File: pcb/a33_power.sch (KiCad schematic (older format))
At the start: 48 parts, among them U3 TPS62095RGTR, U4 TPS62095RGTR, U5 TPS62095RGTR, U6 TPS62095RGTR

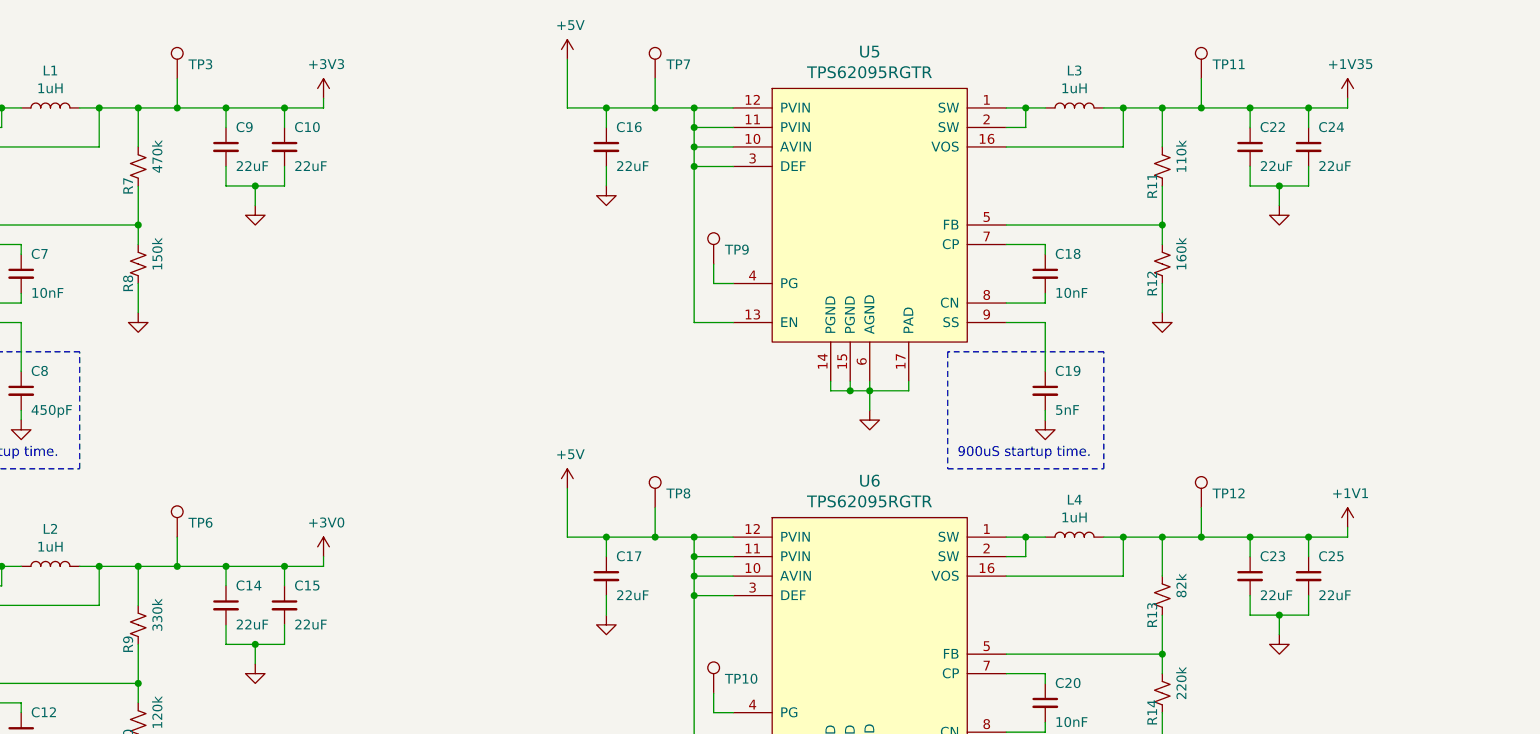
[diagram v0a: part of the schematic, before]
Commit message: Finished up all the switching power supplies.
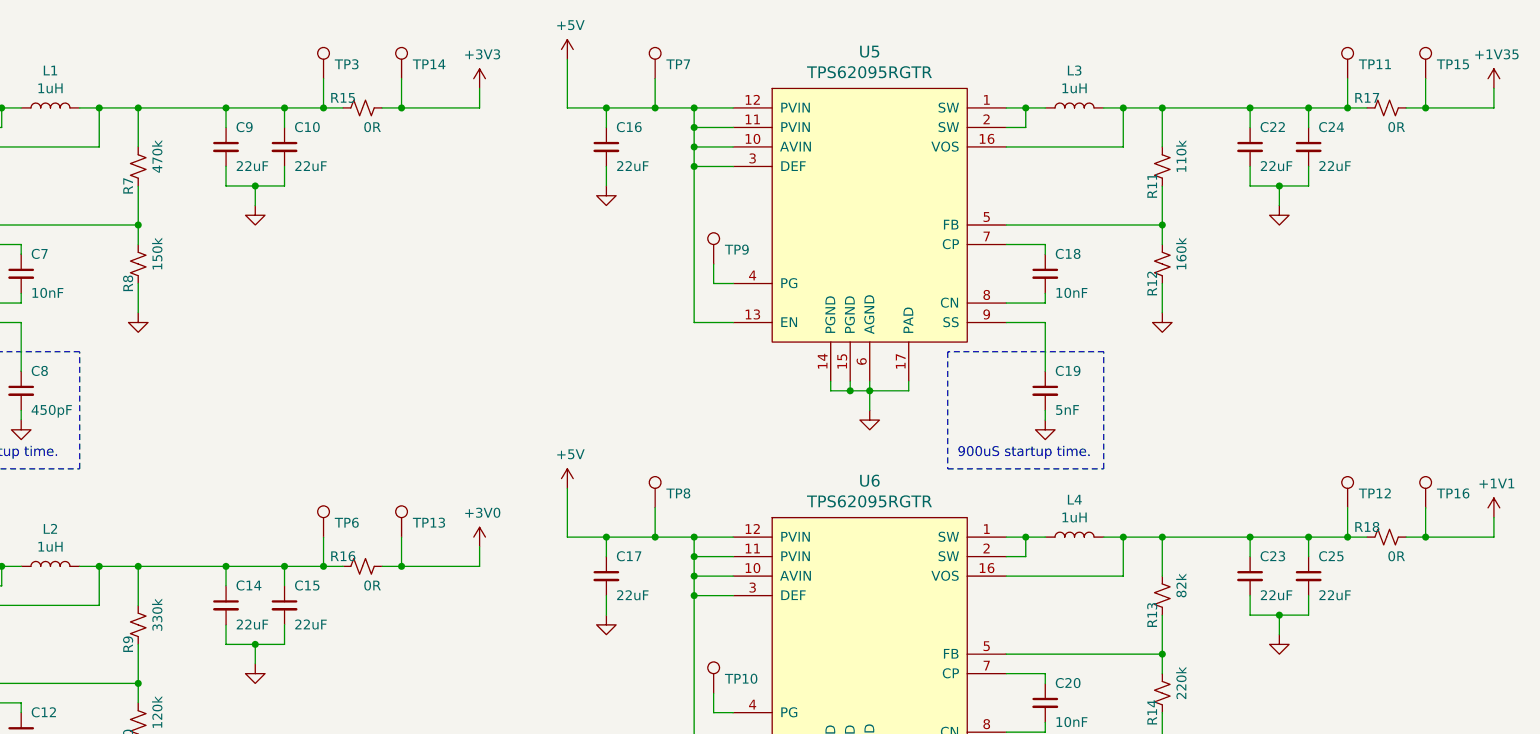
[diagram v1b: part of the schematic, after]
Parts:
- added R15, R16, R17, R18: 0R, Resistor_SMD:R_0402_1005Metric, symbol Device:R_Small_US
- added TP13, TP14, TP15, TP16: TestPoint, symbol Connector:TestPoint
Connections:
- net +1V1: now also R18.1, TP16.1; no longer C23.1, C25.1, L4.2, R13.1, TP12.1, U6.16 (VOS)
- net +1V35: now also R17.1, TP15.1; no longer C22.1, C24.1, L3.2, R11.1, TP11.1, U5.16 (VOS)
- net +3V0: now also R16.1, TP13.1; no longer C14.1, C15.1, L2.2, R9.1, TP6.1, U4.16 (VOS)
- net +3V3: now also R15.1, TP14.1; no longer C10.1, C9.1, L1.2, R7.1, TP3.1, U3.16 (VOS)
- new net: C10.1, C9.1, L1.2, R15.2, R7.1, TP3.1, U3.16 (VOS)
- new net: C14.1, C15.1, L2.2, R16.2, R9.1, TP6.1, U4.16 (VOS)
- new net: C22.1, C24.1, L3.2, R11.1, R17.2, TP11.1, U5.16 (VOS)
- new net: C23.1, C25.1, L4.2, R13.1, R18.2, TP12.1, U6.16 (VOS)
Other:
- moved on the sheet: TP11, TP12, TP3, TP6

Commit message: Added the inductor PN in and dropped them on the board.
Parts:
- L1, L3, L4: footprint (none) -> Inductor_SMD:L_Coilcraft_XxL4020; Part Number (none) -> XAL4020-102ME
- L2: footprint (none) -> Inductor_SMD:L_Coilcraft_XxL4020; Part Nunber (none) -> XAL4020-102ME
- TP1, TP10, TP11, TP12, TP13, TP14, TP15, TP16, TP2, TP3, TP4, TP5, TP6, TP7, TP8, TP9: footprint (none) -> TestPoint:TestPoint_Pad_1.0x1.0mm
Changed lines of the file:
@@
 F 0 "TP2" H 1508 1872 50  0000 L CNN
 F 1 "TestPoint" H 1508 1827 50  0001 L CNN
-F 2 "" H 1650 1800 50  0001 C CNN
+F 2 "TestPoint:TestPoint_Pad_1.0x1.0mm" H 1650 1800 50  0001 C CNN
 F 3 "~" H 1650 1800 50  0001 C CNN
 	1    1450 1800
@@
 F 0 "L1" V 3490 1000 50  0000 C CNN
 F 1 "1uH" V 3399 1000 50  0000 C CNN
-F 2 "" H 3300 1000 50  0001 C CNN
+F 2 "Inductor_SMD:L_Coilcraft_XxL4020" H 3300 1000 50  0001 C CNN
 F 3 "~" H 3300 1000 50  0001 C CNN
+F 4 "XAL4020-102ME" V 3300 1000 50  0001 C CNN "Part Number"
 	1    3300 1000
 	0    -1   -1   0
@@
 F 0 "TP3" H 4758 922 50  0000 L CNN
 F 1 "TestPoint" H 4758 877 50  0001 L CNN
-F 2 "" H 4900 850 50  0001 C CNN
+F 2 "TestPoint:TestPoint_Pad_1.0x1.0mm" H 4900 850 50  0001 C CNN
 F 3 "~" H 4900 850 50  0001 C CNN
 	1    4700 850
@@
 F 0 "TP1" H 1208 922 50  0000 L CNN
 F 1 "TestPoint" H 1208 877 50  0001 L CNN
-F 2 "" H 1350 850 50  0001 C CNN
+F 2 "TestPoint:TestPoint_Pad_1.0x1.0mm" H 1350 850 50  0001 C CNN
 F 3 "~" H 1350 850 50  0001 C CNN
 	1    1150 850
@@
 F 0 "TP5" H 1508 4222 50  0000 L CNN
 F 1 "TestPoint" H 1508 4177 50  0001 L CNN
-F 2 "" H 1650 4150 50  0001 C CNN
+F 2 "TestPoint:TestPoint_Pad_1.0x1.0mm" H 1650 4150 50  0001 C CNN
 F 3 "~" H 1650 4150 50  0001 C CNN
 	1    1450 4150
@@
 F 0 "L2" V 3490 3350 50  0000 C CNN
 F 1 "1uH" V 3399 3350 50  0000 C CNN
-F 2 "" H 3300 3350 50  0001 C CNN
+F 2 "Inductor_SMD:L_Coilcraft_XxL4020" H 3300 3350 50  0001 C CNN
 F 3 "~" H 3300 3350 50  0001 C CNN
+F 4 "XAL4020-102ME" V 3300 3350 50  0001 C CNN "Part Nunber"
 	1    3300 3350
 	0    -1   -1   0
@@
 F 0 "TP6" H 4758 3272 50  0000 L CNN
 F 1 "TestPoint" H 4758 3227 50  0001 L CNN
-F 2 "" H 4900 3200 50  0001 C CNN
+F 2 "TestPoint:TestPoint_Pad_1.0x1.0mm" H 4900 3200 50  0001 C CNN
 F 3 "~" H 4900 3200 50  0001 C CNN
 	1    4700 3200
@@
 F 0 "TP4" H 1208 3272 50  0000 L CNN
 F 1 "TestPoint" H 1208 3227 50  0001 L CNN
-F 2 "" H 1350 3200 50  0001 C CNN
+F 2 "TestPoint:TestPoint_Pad_1.0x1.0mm" H 1350 3200 50  0001 C CNN
 F 3 "~" H 1350 3200 50  0001 C CNN
 	1    1150 3200
@@
 F 0 "TP9" H 6758 1872 50  0000 L CNN
 F 1 "TestPoint" H 6758 1827 50  0001 L CNN
-F 2 "" H 6900 1800 50  0001 C CNN
+F 2 "TestPoint:TestPoint_Pad_1.0x1.0mm" H 6900 1800 50  0001 C CNN
 F 3 "~" H 6900 1800 50  0001 C CNN
 	1    6700 1800
@@
 F 0 "L3" V 8740 1000 50  0000 C CNN
 F 1 "1uH" V 8649 1000 50  0000 C CNN
-F 2 "" H 8550 1000 50  0001 C CNN
+F 2 "Inductor_SMD:L_Coilcraft_XxL4020" H 8550 1000 50  0001 C CNN
 F 3 "~" H 8550 1000 50  0001 C CNN
+F 4 "XAL4020-102ME" V 8550 1000 50  0001 C CNN "Part Number"
 	1    8550 1000
 	0    -1   -1   0
@@
 F 0 "TP11" H 10008 922 50  0000 L CNN
 F 1 "TestPoint" H 10008 877 50  0001 L CNN
-F 2 "" H 10150 850 50  0001 C CNN
+F 2 "TestPoint:TestPoint_Pad_1.0x1.0mm" H 10150 850 50  0001 C CNN
 F 3 "~" H 10150 850 50  0001 C CNN
 	1    9950 850
@@
 F 0 "TP7" H 6458 922 50  0000 L CNN
 F 1 "TestPoint" H 6458 877 50  0001 L CNN
-F 2 "" H 6600 850 50  0001 C CNN
+F 2 "TestPoint:TestPoint_Pad_1.0x1.0mm" H 6600 850 50  0001 C CNN
 F 3 "~" H 6600 850 50  0001 C CNN
 	1    6400 850
@@
 F 0 "TP10" H 6758 4072 50  0000 L CNN
 F 1 "TestPoint" H 6758 4027 50  0001 L CNN
-F 2 "" H 6900 4000 50  0001 C CNN
+F 2 "TestPoint:TestPoint_Pad_1.0x1.0mm" H 6900 4000 50  0001 C CNN
 F 3 "~" H 6900 4000 50  0001 C CNN
 	1    6700 4000
@@
 F 0 "L4" V 8740 3200 50  0000 C CNN
 F 1 "1uH" V 8649 3200 50  0000 C CNN
-F 2 "" H 8550 3200 50  0001 C CNN
+F 2 "Inductor_SMD:L_Coilcraft_XxL4020" H 8550 3200 50  0001 C CNN
 F 3 "~" H 8550 3200 50  0001 C CNN
+F 4 "XAL4020-102ME" V 8550 3200 50  0001 C CNN "Part Number"
 	1    8550 3200
 	0    -1   -1   0
@@
 F 0 "TP12" H 10008 3122 50  0000 L CNN
 F 1 "TestPoint" H 10008 3077 50  0001 L CNN
-F 2 "" H 10150 3050 50  0001 C CNN
+F 2 "TestPoint:TestPoint_Pad_1.0x1.0mm" H 10150 3050 50  0001 C CNN
 F 3 "~" H 10150 3050 50  0001 C CNN
 	1    9950 3050
@@
 F 0 "TP8" H 6458 3122 50  0000 L CNN
 F 1 "TestPoint" H 6458 3077 50  0001 L CNN
-F 2 "" H 6600 3050 50  0001 C CNN
+F 2 "TestPoint:TestPoint_Pad_1.0x1.0mm" H 6600 3050 50  0001 C CNN
 F 3 "~" H 6600 3050 50  0001 C CNN
 	1    6400 3050
@@
 F 0 "TP15" H 10408 922 50  0000 L CNN
 F 1 "TestPoint" H 10408 877 50  0001 L CNN
-F 2 "" H 10550 850 50  0001 C CNN
+F 2 "TestPoint:TestPoint_Pad_1.0x1.0mm" H 10550 850 50  0001 C CNN
 F 3 "~" H 10550 850 50  0001 C CNN
 	1    10350 850
@@
 F 0 "TP16" H 10408 3122 50  0000 L CNN
 F 1 "TestPoint" H 10408 3077 50  0001 L CNN
-F 2 "" H 10550 3050 50  0001 C CNN
+F 2 "TestPoint:TestPoint_Pad_1.0x1.0mm" H 10550 3050 50  0001 C CNN
 F 3 "~" H 10550 3050 50  0001 C CNN
 	1    10350 3050
@@
 F 0 "TP13" H 5158 3272 50  0000 L CNN
 F 1 "TestPoint" H 5158 3227 50  0001 L CNN
-F 2 "" H 5300 3200 50  0001 C CNN
+F 2 "TestPoint:TestPoint_Pad_1.0x1.0mm" H 5300 3200 50  0001 C CNN
 F 3 "~" H 5300 3200 50  0001 C CNN
 	1    5100 3200
@@
 F 0 "TP14" H 5158 922 50  0000 L CNN
 F 1 "TestPoint" H 5158 877 50  0001 L CNN
-F 2 "" H 5300 850 50  0001 C CNN
+F 2 "TestPoint:TestPoint_Pad_1.0x1.0mm" H 5300 850 50  0001 C CNN
 F 3 "~" H 5300 850 50  0001 C CNN
 	1    5100 850

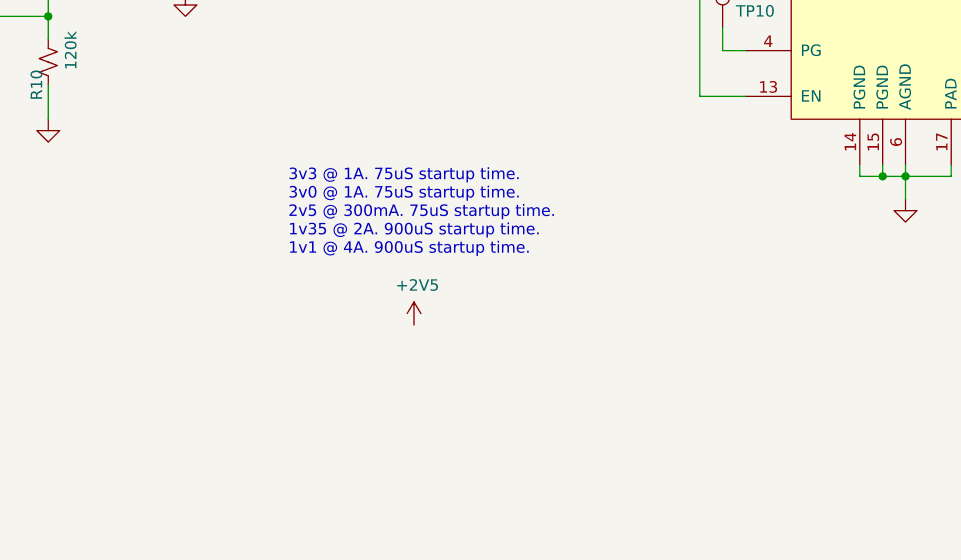
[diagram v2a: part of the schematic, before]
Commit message: Added the 2.5V LDO
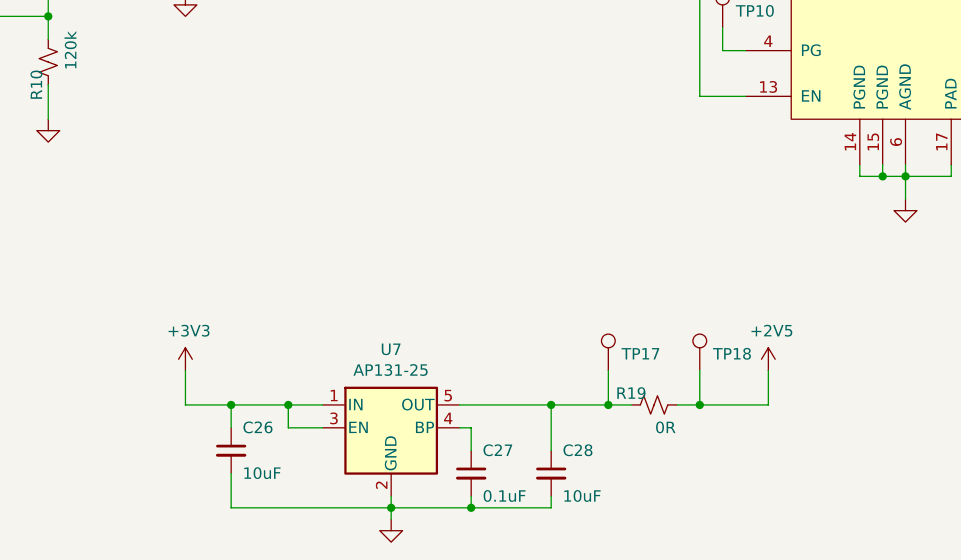
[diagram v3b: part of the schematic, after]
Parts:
- added C26, C28: 10uF, Capacitor_SMD:C_01005_0402Metric, symbol Device:C_Small
- added C27: 0.1uF, Capacitor_SMD:C_01005_0402Metric, symbol Device:C_Small
- added R19: 0R, Resistor_SMD:R_0402_1005Metric, symbol Device:R_Small_US
- added TP17, TP18: TestPoint, TestPoint:TestPoint_Pad_1.0x1.0mm, symbol Connector:TestPoint
- added U7: AP131-25, Package_TO_SOT_SMD:SOT-23-5, symbol Regulator_Linear:AP131-25
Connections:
- net +2V5: now also R19.1, TP18.1
- net +3V3: now also C26.1, U7.1 (IN), U7.3 (EN)
- net GND: now also C26.2, C27.2, C28.2, U7.2 (GND)
- new net: C27.1, U7.4 (BP)
- new net: C28.1, R19.2, TP17.1, U7.5 (OUT)
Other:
- note removed: "3v3 @ 1A. 75uS startup time.\n3v0 @ 1A. 75uS startup time.\n2v5 @ 300mA. 75uS startup time.\n1v35 @ 2A. 900uS startup time.\n1v1 @ 4A. 900uS startup time."
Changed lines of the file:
@@
 $EndDescr
-$Comp
-L power:+2V5 #PWR06
-U 1 1 605379DF
-P 5350 5300
-F 0 "#PWR06" H 5350 5150 50  0001 C CNN
-F 1 "+2V5" H 5365 5473 50  0000 C CNN
-F 2 "" H 5350 5300 50  0001 C CNN
-F 3 "" H 5350 5300 50  0001 C CNN
-	1    5350 5300
-	1    0    0    -1
-$EndComp
-Text Notes 4800 5000 0    50   ~ 0
-3v3 @ 1A. 75uS startup time.\n3v0 @ 1A. 75uS startup time.\n2v5 @ 300mA. 75uS startup time.\n1v35 @ 2A. 900uS startup time.\n1v1 @ 4A. 900uS startup time.
 $Comp
 L power:+5V #PWR019
@@
 Wire Wire Line
 	10350 3200 10700 3200
+$Comp
+L Regulator_Linear:AP131-25 U7
+U 1 1 60A041CF
+P 5250 5750
+F 0 "U7" H 5250 6092 50  0000 C CNN
+F 1 "AP131-25" H 5250 6001 50  0000 C CNN
+F 2 "Package_TO_SOT_SMD:SOT-23-5" H 5250 6075 50  0001 C CNN
+F 3 "http://www.diodes.com/_files/datasheets/AP131.pdf" H 5250 5750 50  0001 C CNN
+	1    5250 5750
+	1    0    0    -1
+$EndComp
+$Comp
+L Device:C_Small C?
+U 1 1 60A109D4
+P 5950 5950
+AR Path="/60536DA4/60A109D4" Ref="C?"  Part="1"
+AR Path="/60A30BFF/60A109D4" Ref="C28"  Part="1"
+F 0 "C28" H 6000 6050 50  0000 L CNN
+F 1 "10uF" H 6000 5850 50  0000 L CNN
+F 2 "Capacitor_SMD:C_01005_0402Metric" H 5950 5950 50  0001 C CNN
+F 3 "~" H 5950 5950 50  0001 C CNN
+	1    5950 5950
+	1    0    0    -1
+$EndComp
+$Comp
+L Device:C_Small C?
+U 1 1 60A116E2
+P 5600 5950
+AR Path="/60536DA4/60A116E2" Ref="C?"  Part="1"
+AR Path="/60A30BFF/60A116E2" Ref="C27"  Part="1"
+F 0 "C27" H 5650 6050 50  0000 L CNN
+F 1 "0.1uF" H 5650 5850 50  0000 L CNN
+F 2 "Capacitor_SMD:C_01005_0402Metric" H 5600 5950 50  0001 C CNN
+F 3 "~" H 5600 5950 50  0001 C CNN
+	1    5600 5950
+	1    0    0    -1
+$EndComp
+$Comp
+L Device:C_Small C?
+U 1 1 60A11ECD
+P 4550 5850
+AR Path="/60536DA4/60A11ECD" Ref="C?"  Part="1"
+AR Path="/60A30BFF/60A11ECD" Ref="C26"  Part="1"
+F 0 "C26" H 4600 5950 50  0000 L CNN
+F 1 "10uF" H 4600 5750 50  0000 L CNN
+F 2 "Capacitor_SMD:C_01005_0402Metric" H 4550 5850 50  0001 C CNN
+F 3 "~" H 4550 5850 50  0001 C CNN
+	1    4550 5850
+	1    0    0    -1
+$EndComp
+Wire Wire Line
+	4950 5650 4800 5650
+Wire Wire Line
+	4350 5650 4350 5500
+$Comp
+L power:+3V3 #PWR06
+U 1 1 60A23846
+P 4350 5500
+F 0 "#PWR06" H 4350 5350 50  0001 C CNN
+F 1 "+3V3" H 4365 5673 50  0000 C CNN
+F 2 "" H 4350 5500 50  0001 C CNN
+F 3 "" H 4350 5500 50  0001 C CNN
+	1    4350 5500
+	1    0    0    -1
+$EndComp
+Wire Wire Line
+	4550 5750 4550 5650
+Connection ~ 4550 5650
+Wire Wire Line
+	4550 5650 4350 5650
+Wire Wire Line
+	5550 5750 5600 5750
+Wire Wire Line
+	5600 5750 5600 5850
+Wire Wire Line
+	5600 6050 5600 6100
+$Comp
+L power:GND #PWR?
+U 1 1 60A54975
+P 5250 6150
+AR Path="/60536DA4/60A54975" Ref="#PWR?"  Part="1"
+AR Path="/60A54975" Ref="#PWR?"  Part="1"
+AR Path="/60A30BFF/60A54975" Ref="#PWR044"  Part="1"
+F 0 "#PWR044" H 5250 5900 50  0001 C CNN
+F 1 "GND" V 5255 6022 50  0001 R CNN
+F 2 "" H 5250 6150 50  0001 C CNN
+F 3 "" H 5250 6150 50  0001 C CNN
+	1    5250 6150
+	1    0    0    -1
+$EndComp
+Wire Wire Line
+	5250 6150 5250 6100
+Wire Wire Line
+	5950 5650 5950 5850
+Wire Wire Line
+	5550 5650 5950 5650
+Wire Wire Line
+	5950 6050 5950 6100
+Wire Wire Line
+	5950 6100 5600 6100
+Wire Wire Line
+	4550 6100 4550 5950
+Connection ~ 5250 6100
+Wire Wire Line
+	5250 6100 5250 6050
+Wire Wire Line
+	5250 6100 4550 6100
+Connection ~ 5600 6100
+Wire Wire Line
+	5600 6100 5250 6100
+Wire Wire Line
+	5950 5650 6200 5650
+Wire Wire Line
+	6900 5650 6900 5500
+Connection ~ 5950 5650
+$Comp
+L power:+2V5 #PWR045
+U 1 1 60AD6A4A
+P 6900 5500
+F 0 "#PWR045" H 6900 5350 50  0001 C CNN
+F 1 "+2V5" H 6915 5673 50  0000 C CNN
+F 2 "" H 6900 5500 50  0001 C CNN
+F 3 "" H 6900 5500 50  0001 C CNN
+	1    6900 5500
+	1    0    0    -1
+$EndComp
+$Comp
+L Device:R_Small_US R?
+U 1 1 60AF9B3F
+P 6400 5650
+AR Path="/60536DA4/60AF9B3F" Ref="R?"  Part="1"
+AR Path="/60AF9B3F" Ref="R?"  Part="1"
+AR Path="/60A30BFF/60AF9B3F" Ref="R19"  Part="1"
+F 0 "R19" V 6350 5550 50  0000 C CNN
+F 1 "0R" V 6500 5700 50  0000 C CNN
+F 2 "Resistor_SMD:R_0402_1005Metric" H 6400 5650 50  0001 C CNN
+F 3 "~" H 6400 5650 50  0001 C CNN
+	1    6400 5650
+	0    1    1    0
+$EndComp
+Wire Wire Line
+	6500 5650 6600 5650
+$Comp
+L Connector:TestPoint TP17
+U 1 1 60B002CC
+P 6200 5500
+F 0 "TP17" H 6258 5572 50  0000 L CNN
+F 1 "TestPoint" H 6258 5527 50  0001 L CNN
+F 2 "TestPoint:TestPoint_Pad_1.0x1.0mm" H 6400 5500 50  0001 C CNN
+F 3 "~" H 6400 5500 50  0001 C CNN
+	1    6200 5500
+	1    0    0    -1
+$EndComp
+Wire Wire Line
+	6200 5650 6200 5500
+$Comp
+L Connector:TestPoint TP18
+U 1 1 60B002D3
+P 6600 5500
+F 0 "TP18" H 6658 5572 50  0000 L CNN
+F 1 "TestPoint" H 6658 5527 50  0001 L CNN
+F 2 "TestPoint:TestPoint_Pad_1.0x1.0mm" H 6800 5500 50  0001 C CNN
+F 3 "~" H 6800 5500 50  0001 C CNN
+	1    6600 5500
+	1    0    0    -1
+$EndComp
+Wire Wire Line
+	6600 5650 6600 5500
+Connection ~ 6600 5650
+Wire Wire Line
+	6600 5650 6900 5650
+Connection ~ 6200 5650
+Wire Wire Line
+	6200 5650 6300 5650
+Wire Wire Line
+	4950 5750 4800 5750
+Wire Wire Line
+	4800 5750 4800 5650
+Connection ~ 4800 5650
+Wire Wire Line
+	4800 5650 4550 5650
 $EndSCHEMATC
